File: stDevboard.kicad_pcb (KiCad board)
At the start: 4 copper layers, 50 x 100 mm, 143 parts, among them IC1 MPM3610GQV-Z, IC2 IRFR9014PBF, IC3 ICM-45686, IC4 ICM-45686, IC5 MMC5983MA, IC6 AT25SF041B-SSHB-B, J1 battery, J10 73412-0114, J11 USB_C_Receptacle_USB2.0_16P, J12 73412-0114, J13 Conn_01x04, J14 Micro_SD_Card_Det2, J2 USB_C_Receptacle_USB2.0_16P, J3 Conn_02x03_Top_Bottom, J4 Screw_Terminal_01x02, J5 Screw_Terminal_01x02, J6 Screw_Terminal_01x02, J7 Screw_Terminal_01x02, J8 Screw_Terminal_01x02, J9 Screw_Terminal_01x02, Q1 IRLML6244, Q2 IRLML6244, Q3 IRLML6244, Q4 IRLML6244, Q5 IRLML6244, Q6 IRLML6244, U1 STM32U073CCUx, U2 STM32U585CIUxQ, U3 BMP581, U4 MAX-M10S, Y1 ECS-160-8-36B2-CKM-TR, Y2 CM7V-T1A-32.768KHZ, Y3 ECS-TXO-25CSMV-320-AM-TR, Y4 CM7V-T1A-32.768KHZ

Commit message: mosfet schematic done I hope
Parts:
- removed D1, D2, D3: D, Diode_SMD:D_0603_1608Metric
- removed Q6: IRLML6244, Package_TO_SOT_SMD:SOT-23
- added Q7: MMBT2222A, Package_TO_SOT_SMD:SOT-23, F.Cu at (180.3, 38.0)
- added Q8: DMN3404L, Package_TO_SOT_SMD:SOT-23, F.Cu at (180.3, 42.4)
- added R29: 1k, Resistor_SMD:R_0402_1005Metric, F.Cu at (184.2, 44.8)
- added R30: 100, Resistor_SMD:R_0603_1608Metric, F.Cu at (188.8, 42.6)
- Q1, Q2, Q3, Q4, Q5: value IRLML6244 -> DMN3404L
- R14: value 1k -> 100k; footprint Resistor_SMD:R_0805_2012Metric -> Resistor_SMD:R_0603_1608Metric
- R16: value 100 -> 1k
- R17: value 100 -> 12k
- R19: value 100 -> 3k
- moved R19 163.5 mm to (188.8, 32.5)
- moved R20 163.5 mm to (188.8, 35.0)
- moved R21 163.5 mm to (188.8, 37.6)
- moved R22 163.5 mm to (188.8, 40.1)
- moved R15 159.8 mm to (184.7, 35.0)
- moved R16 159.8 mm to (184.7, 37.6)
- moved R17 159.8 mm to (184.7, 40.1)
- moved R18 159.8 mm to (184.7, 42.6)
- moved Q5 159.7 mm to (180.3, 33.5)
- moved Q1 154.8 mm to (175.4, 33.5)
- moved Q2 154.8 mm to (175.4, 38.0)
- moved Q3 154.8 mm to (175.4, 42.4)
- moved Q4 154.8 mm to (175.4, 46.9)
- moved R14 151.2 mm to (184.7, 32.5)
- moved J5 139.1 mm to (183.1, 26.6), turned to 0 degrees
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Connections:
- IC2 pad 4: cont_test_in -> +12C
- J4 pad 1: cont_test_in -> +12C
- J4 pad 2: cont_test_out -> Net-(J4-Pin_2)
- J5 pad 1: cont_test_in -> +12C
- J5 pad 2: cont_test_out -> Net-(J5-Pin_2)
- J6 pad 1: cont_test_in -> +12C
- J6 pad 2: cont_test_out -> Net-(J6-Pin_2)
- J7 pad 1: cont_test_in -> +12C
- J7 pad 2: cont_test_out -> Net-(J7-Pin_2)
- J8 pad 1: cont_test_in -> +12C
- J8 pad 2: cont_test_out -> Net-(J8-Pin_2)
- J9 pad 1: cont_test_in -> +12C
- J9 pad 2: cont_test_out -> Net-(J9-Pin_2)
- Q1 pad 3: cont_test_out -> Net-(J5-Pin_2)
- Q2 pad 3: cont_test_out -> Net-(J6-Pin_2)
- Q3 pad 3: cont_test_out -> Net-(J7-Pin_2)
- Q4 pad 3: cont_test_out -> Net-(J8-Pin_2)
- Q5 pad 3: cont_test_out -> Net-(J9-Pin_2)
- R14 pad 1: cont_test_out -> +12C
- R14 pad 2: Net-(D1-K) -> +3.3V
- R16 pad 1: Net-(Q1-G) -> Net-(Q8-G)
- R17 pad 1: cont_test_in -> cont_test_out
- R17 pad 2: Net-(D3-K) -> +12C
- R18 pad 1: Net-(Q2-G) -> Net-(Q1-G)
- R19 pad 1: Net-(Q3-G) -> GND
- R19 pad 2: c3_fire -> cont_test_out
- R20 pad 1: Net-(Q4-G) -> Net-(Q2-G)
- R20 pad 2: c4_fire -> c3_fire
- R21 pad 1: Net-(Q5-G) -> Net-(Q3-G)
- R21 pad 2: c5_fire -> c4_fire
- R22 pad 1: Net-(Q6-G) -> Net-(Q4-G)
- R22 pad 2: c6_fire -> c5_fire
- U1 pad 11: unconnected-(U1-PA1-Pad11) -> cont_test_out
- U1 pad 21: unconnected-(U1-PB10-Pad21) -> c5_fire
- U1 pad 22: unconnected-(U1-PB11-Pad22) -> c6_fire
- U1 pad 29: unconnected-(U1-PA8-Pad29) -> arm
- U1 pad 42: unconnected-(U1-PB6-Pad42) -> c1_fire
- U1 pad 43: unconnected-(U1-PB7-Pad43) -> c2_fire
- U1 pad 45: unconnected-(U1-PB8-Pad45) -> c3_fire
- U1 pad 46: unconnected-(U1-PB9-Pad46) -> c4_fire
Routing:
- net GND: track 191.4 -> 204.8 mm, vias 127 -> 141
- net telem_rst: track 67.6 -> 67.0 mm

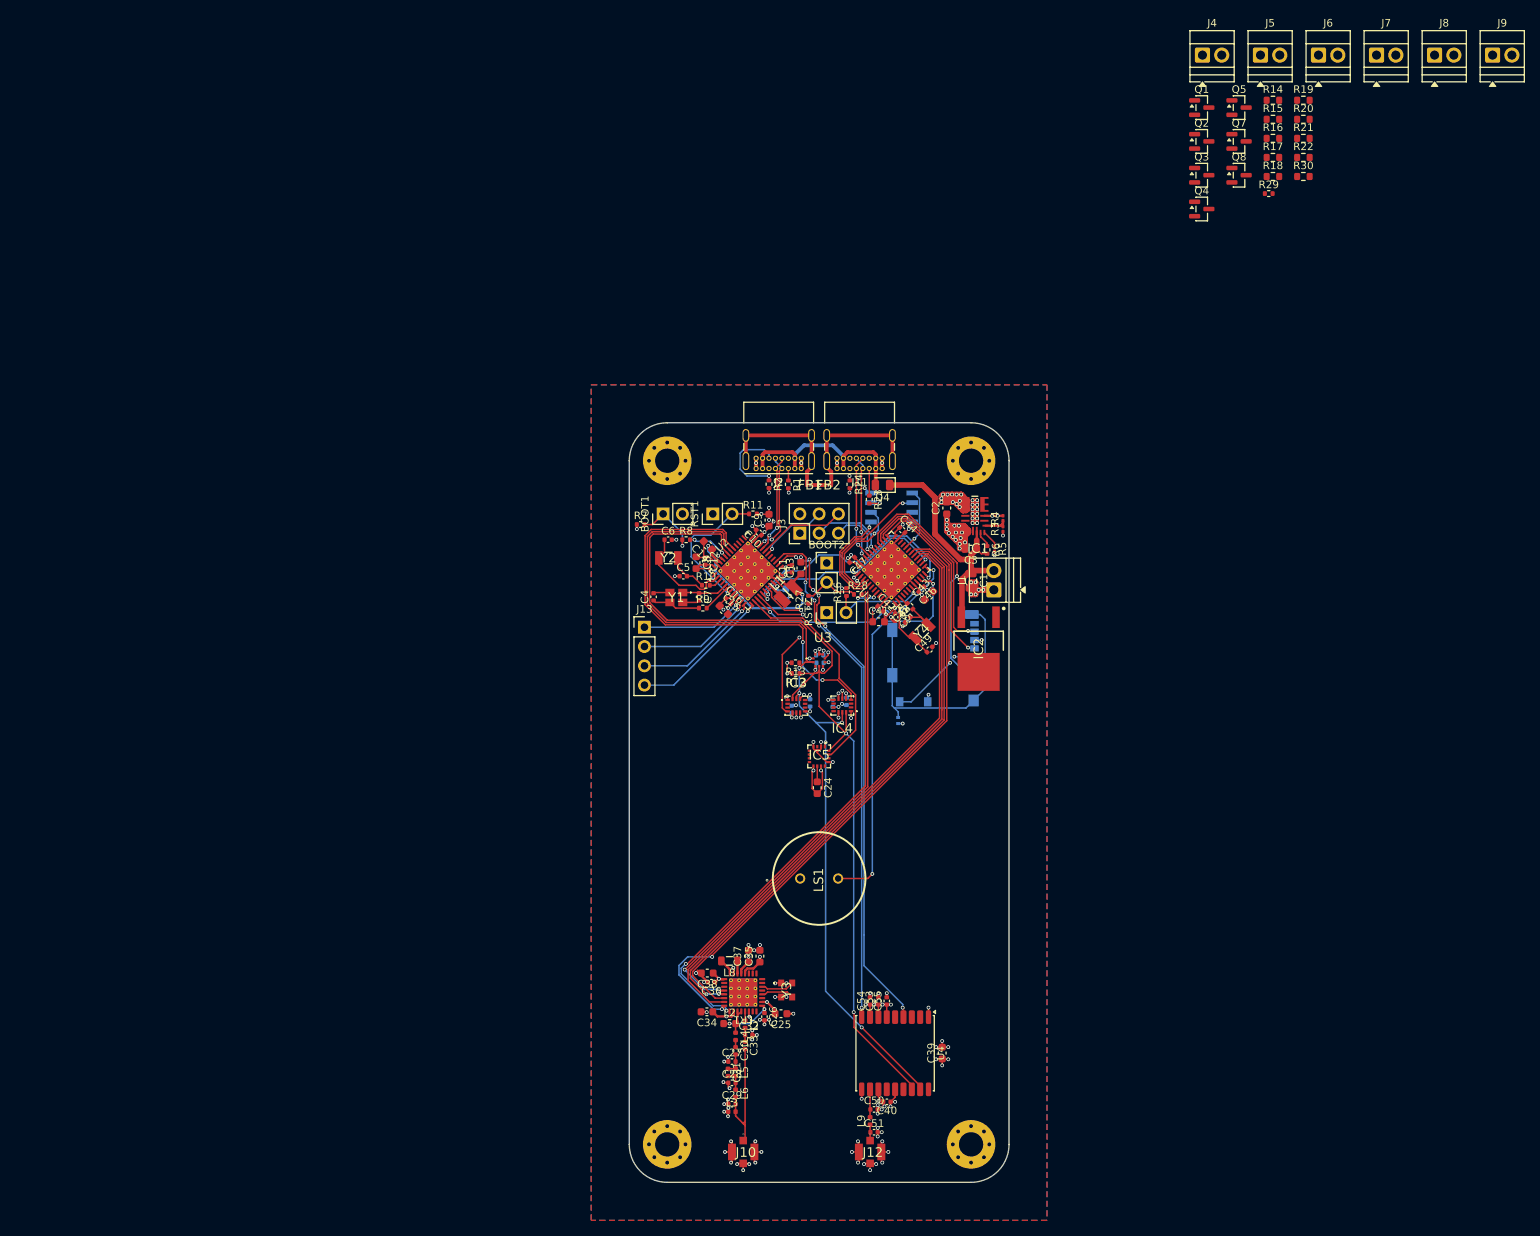
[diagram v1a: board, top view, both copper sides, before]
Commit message: placed mosfet stuff, probably all that's left is add pull resistors on the nfets and finish routing the fets
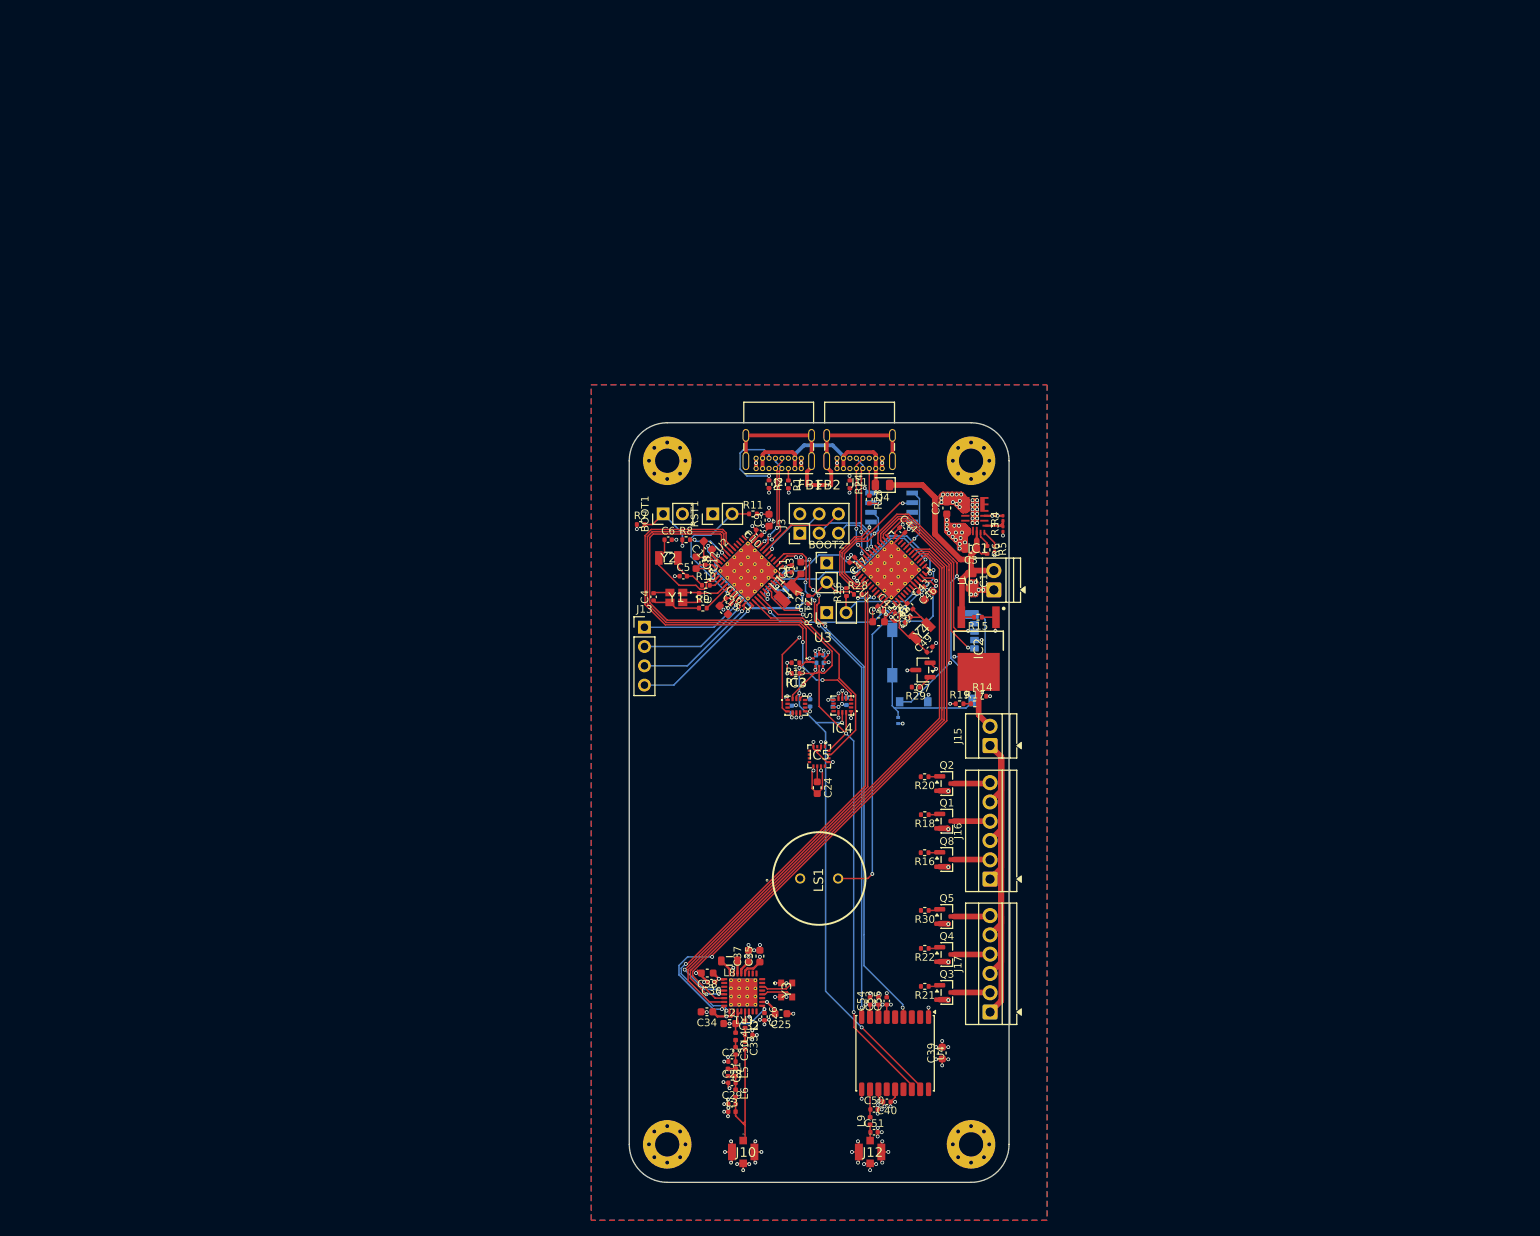
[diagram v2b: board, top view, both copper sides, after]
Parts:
- removed J4, J5, J6, J7, J8, J9: Screw_Terminal_01x02, TerminalBlock:TerminalBlock_Xinya_XY308-2.54-2P_1x02_P2.54mm_Horizontal
- added J15: Arm, TerminalBlock:TerminalBlock_Xinya_XY308-2.54-2P_1x02_P2.54mm_Horizontal, F.Cu at (147.5, 117.5)
- added J16: Screw_Terminal_01x06, TerminalBlock:TerminalBlock_Xinya_XY308-2.54-6P_1x06_P2.54mm_Horizontal, F.Cu at (147.5, 135.1)
- added J17: Screw_Terminal_01x06, TerminalBlock:TerminalBlock_Xinya_XY308-2.54-6P_1x06_P2.54mm_Horizontal, F.Cu at (147.5, 152.6)
- R14, R15, R16, R17, R19: footprint Resistor_SMD:R_0603_1608Metric -> Resistor_SMD:R_0402_1005Metric
- R18, R20, R21, R22, R30: value 100 -> 1k; footprint Resistor_SMD:R_0603_1608Metric -> Resistor_SMD:R_0402_1005Metric
- moved R21 122.3 mm to (138.9, 149.2), turned to 180 degrees
- moved R22 115.4 mm to (138.9, 144.2), turned to 180 degrees
- moved Q5 113.2 mm to (141.8, 140.0)
- moved Q3 112.7 mm to (141.8, 150.0)
- moved R30 108.7 mm to (138.9, 139.2), turned to 180 degrees
- moved R16 104.6 mm to (138.9, 131.6), turned to 180 degrees
- moved Q4 103.7 mm to (141.8, 145.0)
- moved R20 99.9 mm to (138.9, 121.6), turned to 180 degrees
- moved Q1 99.8 mm to (141.8, 127.5)
- moved Q8 98.0 mm to (141.8, 132.5)
- moved R18 95.7 mm to (138.9, 126.6), turned to 180 degrees
- moved R19 91.4 mm to (143.5, 112.0)
- moved Q2 91.0 mm to (141.8, 122.5)
- moved R14 87.3 mm to (146.5, 111.0)
- moved R17 81.9 mm to (145.5, 112.0)
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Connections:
- net +12C renamed Net-(IC2-D)
- Q1 pad 3: Net-(J5-Pin_2) -> /mosfets/c2_n
- Q2 pad 3: Net-(J6-Pin_2) -> /mosfets/c3_n
- Q3 pad 3: Net-(J7-Pin_2) -> /mosfets/c4_n
- Q4 pad 3: Net-(J8-Pin_2) -> /mosfets/c5_n
- Q5 pad 3: Net-(J9-Pin_2) -> /mosfets/c6_n
- Q8 pad 3: Net-(J4-Pin_2) -> /mosfets/c1_n
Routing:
- net +12C: track 0.00 -> 103.4 mm
- net Net-(IC2-G): track 0.00 -> 14.9 mm, vias 0 -> 2
- net GND: track 204.8 -> 213.6 mm, vias 141 -> 149
- net Net-(IC2-D): track 0.00 -> 7.78 mm
- net /mosfets/c6_n: track 0.00 -> 4.80 mm
- net /mosfets/c3_n: track 0.00 -> 4.80 mm
- net /mosfets/c5_n: track 0.00 -> 4.77 mm
- net /mosfets/c4_n: track 0.00 -> 4.77 mm
- net /mosfets/c1_n: track 0.00 -> 4.77 mm
- net /mosfets/c2_n: track 0.00 -> 4.75 mm
- net cont_test_out: track 0.00 -> 3.09 mm, vias 0 -> 1
- net Net-(Q7-B): track 0.00 -> 1.92 mm
- net +BATT: track 34.8 -> 36.5 mm
- net Net-(Q5-G): track 0.00 -> 1.52 mm
- net Net-(Q4-G): track 0.00 -> 1.52 mm
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
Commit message: idk what I did but it wasn't saved
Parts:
- removed J16, J17: Screw_Terminal_01x06, TerminalBlock:TerminalBlock_Xinya_XY308-2.54-6P_1x06_P2.54mm_Horizontal
- added J4: Screw_Terminal_01x12, TerminalBlock:TerminalBlock_Xinya_XY308-2.54-12P_1x12_P2.54mm_Horizontal, F.Cu at (147.5, 150.1)
- C1, C3, R15: moved to B.Cu
- R3, R4, R5: footprint Resistor_SMD:R_0201_0603Metric -> Resistor_SMD:R_0402_1005Metric; moved to B.Cu
- moved Q2 12.5 mm to (141.9, 135.0)
- moved R20 12.5 mm to (138.9, 134.1)
- moved R30 10.2 mm to (139.0, 149.4)
- moved Q5 10.2 mm to (141.9, 150.2)
- moved Q3 10.0 mm to (141.9, 140.0)
- moved R21 10.0 mm to (139.0, 139.2)
- moved Q8 7.70 mm to (141.9, 124.8)
- moved R16 7.70 mm to (138.9, 123.9)
- moved R18 2.55 mm to (139.0, 129.2)
- moved Q1 2.55 mm to (141.9, 130.0)
- moved R15 2.34 mm to (148.2, 101.1), turned to 90 degrees
- moved R5 1.30 mm to (147.0, 90.9)
- moved R3 0.99 mm to (148.3, 89.5)
- moved R4 0.85 mm to (148.3, 87.5)
- moved J1 0.52 mm to (147.5, 96.8)
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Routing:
- net +12C: track 103.4 -> 44.9 mm
- net cont_test_out: track 3.09 -> 21.0 mm, vias 1 -> 2
- net +BATT: track 36.5 -> 47.3 mm
- net GND: track 213.6 -> 208.5 mm, vias 149 -> 145
- net +3.3V: track 107.8 -> 109.5 mm
- net Net-(IC1-AAM): track 2.38 -> 1.26 mm, vias 0 -> 1
- net Net-(IC2-G): track 14.9 -> 13.9 mm
- net /peripheral micro/sd_mosi: track 32.1 -> 31.0 mm
- net Net-(IC1-FB): track 3.92 -> 3.02 mm, vias 0 -> 1
- net Net-(IC1-EN): track 2.13 -> 2.78 mm

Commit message: almost done routing! getting pretty close to done now
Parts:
- added Q6: MMBT2222A, Package_TO_SOT_SMD:SOT-23, F.Cu at (133.3, 133.9)
- added R31: 1k, Resistor_SMD:R_0402_1005Metric, F.Cu at (132.4, 131.3)
- U1, U2: footprint Package_DFN_QFN:QFN-48-1EP_7x7mm_P0.5mm_EP5.6x5.6mm_ThermalVias -> Package_DFN_QFN:QFN-48-1EP_7x7mm_P0.5mm_EP5.6x5.6mm
- moved D4 4.12 mm to (137.5, 83.2)
- moved R23 4.12 mm to (135.2, 83.1)
- moved R2 4.00 mm to (114.4, 83.1)
- moved J11 4.00 mm to (137.3, 81.0)
- moved J2 4.00 mm to (118.7, 81.0)
- moved R24 3.95 mm to (133.0, 83.1)
- moved R1 3.48 mm to (117.5, 82.6), turned to 0 degrees
- moved FB1 2.69 mm to (121.8, 81.4), turned to -90 degrees
- moved FB2 2.69 mm to (128.2, 81.4), turned to -90 degrees
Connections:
- LS1 pad 1: GND -> +3.3V
- LS1 pad 2: Net-(U1-PA0) -> Net-(Q6-E)
- U4 pad 5: unconnected-(U4-EXTINT-Pad5) -> gps_int
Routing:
- net gps_int: track 0.80 -> 71.7 mm, vias 1 -> 4
- net c4_fire: track 0.00 -> 47.6 mm, vias 0 -> 3
- net c3_fire: track 0.00 -> 42.6 mm, vias 0 -> 3
- net c2_fire: track 0.00 -> 38.9 mm, vias 0 -> 3
- net arm: track 0.00 -> 38.8 mm, vias 0 -> 3
- net c1_fire: track 0.00 -> 32.2 mm, vias 0 -> 3
- net c6_fire: track 0.00 -> 31.7 mm, vias 0 -> 2
- net c5_fire: track 0.00 -> 26.9 mm, vias 0 -> 2
- net Net-(U1-PA0): track 52.0 -> 44.2 mm
- net +5V: track 26.7 -> 33.6 mm
- net GND: track 208.5 -> 214.7 mm, vias 145 -> 143
- net Net-(Q6-E): track 0.00 -> 4.94 mm
- net +BATT: track 47.3 -> 43.1 mm
- net Net-(J2-CC2): track 11.6 -> 7.58 mm
- net Net-(J11-CC2): track 11.0 -> 7.54 mm
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- added copper zone on In2.Cu, net +3.3V
- added copper zone on In1.Cu, net GND
- removed copper zone on In1.Cu, net +3.3V
- removed copper zone on In2.Cu, net GND

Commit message: routing done! silkscreen is probably good enough for now
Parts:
- renumbered J15 to ARM, U3 to BARO, BOOT2 to BOOT, BOOT1 to BOOT, U4 to GPS, IC3 to IMU1, IC4 to IMU2, IC5 to MAG, LS1 to PIEZO, RST2 to RST, RST1 to RST, J13 to SERVO, LR1 to TELEM, J3 to UART
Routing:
- net c6_fire: track 31.7 -> 76.6 mm, vias 2 -> 3
- net c5_fire: track 26.9 -> 70.3 mm, vias 2 -> 3
- net GND: track 214.7 -> 220.5 mm

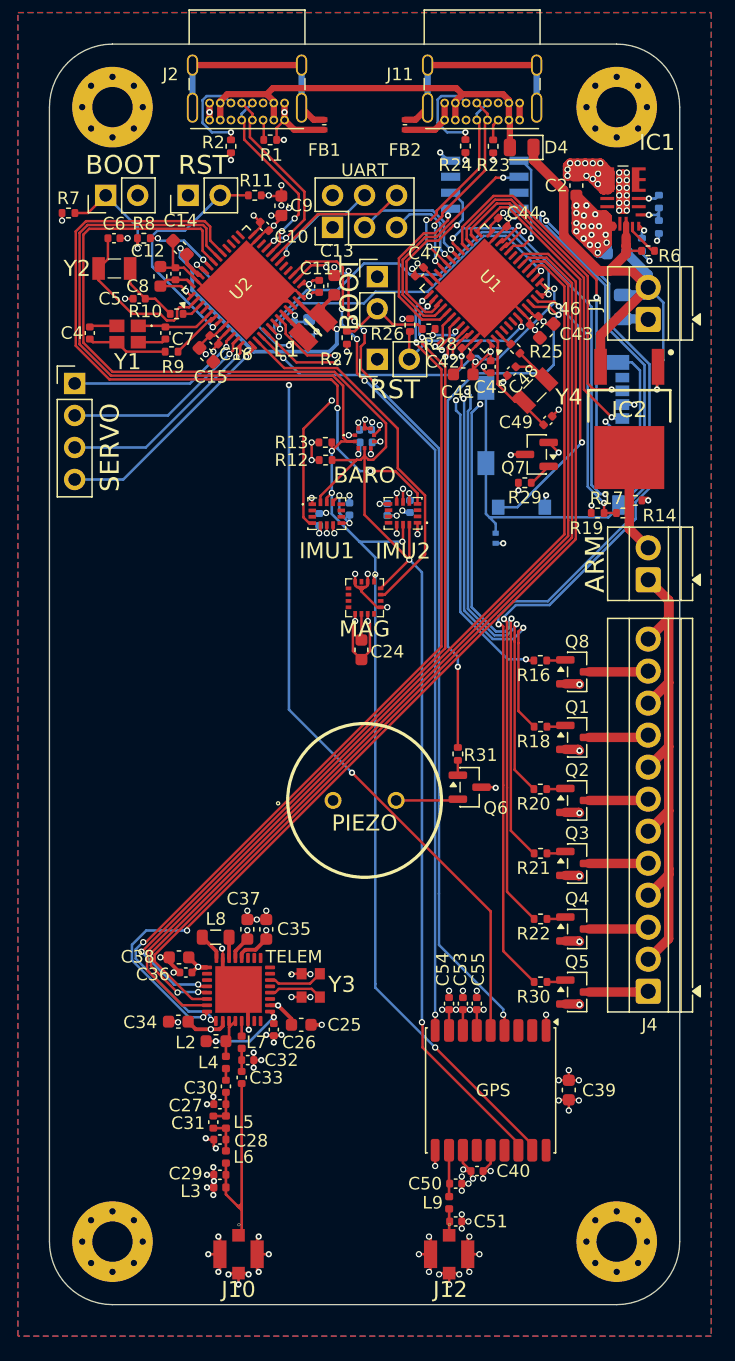
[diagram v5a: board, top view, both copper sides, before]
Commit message: stiching and fencing vias, fixed via diameters
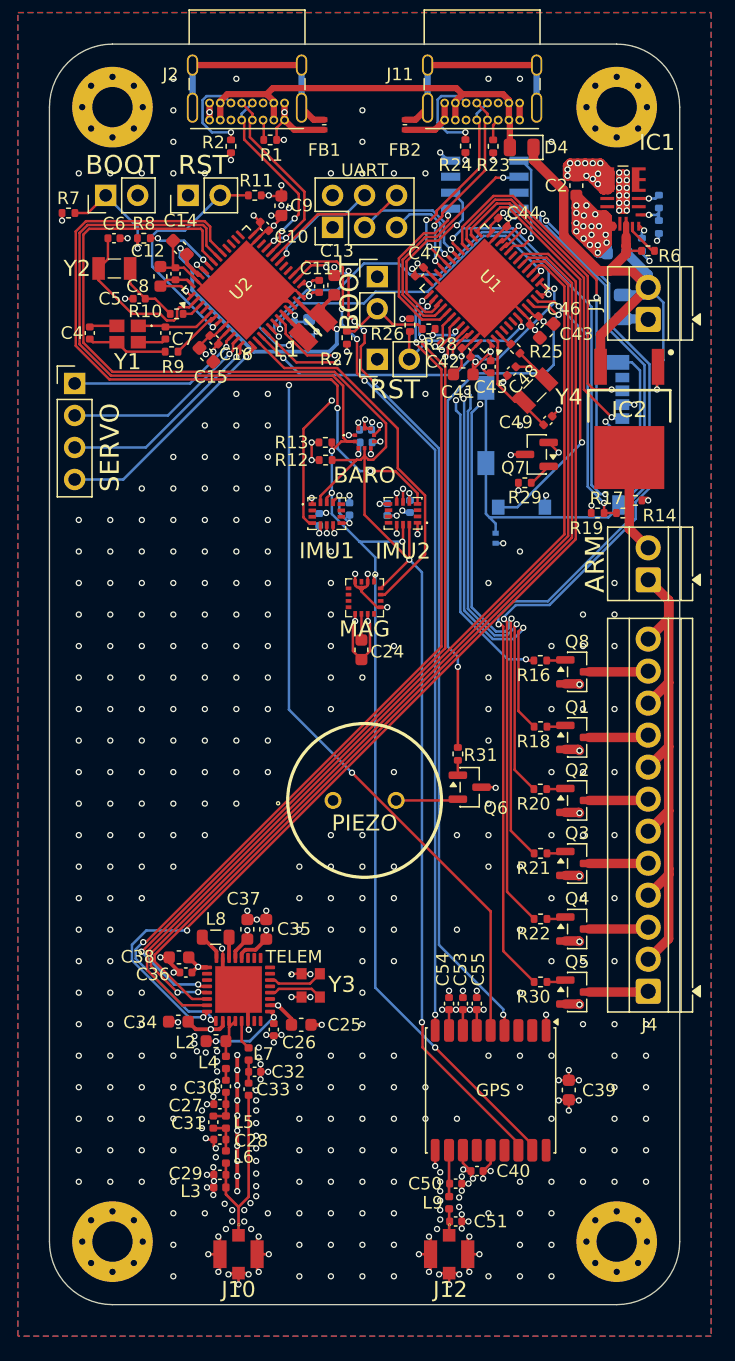
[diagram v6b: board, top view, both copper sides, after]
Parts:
- moved C32 1.08 mm to (116.3, 156.5)
- moved C33 1.08 mm to (115.8, 157.9)
- moved L7 1.08 mm to (115.8, 155.1)
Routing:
- net GND: track 220.5 -> 231.3 mm, vias 143 -> 471
- net Net-(J10-SIGNAL): track 17.0 -> 15.3 mm
- net Net-(LR1-RFI_LF): track 1.20 -> 2.36 mm
